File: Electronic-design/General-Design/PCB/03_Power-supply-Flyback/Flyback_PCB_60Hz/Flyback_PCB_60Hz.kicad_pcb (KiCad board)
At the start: 2 copper layers, 150 x 114.2 mm, 88 parts, among them IC1 TPS54302DDCR, IC2 L7812CV, IC3 L7912CV, IC4 DPC817L-A-TR, IC5 UCC38C43DR, IC6 TL431ACLPR, J1 4300.0104, J2 -12V, J3 +12V, J4 +5V, J5 TB002-500-02BE, Q1 BFR182E6327HTSA1, Q3 2N3906BU, Q4 Q_NMOS_GDS, T1 3FS-324, T3 750811351

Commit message: Flyback-PCB-Final1
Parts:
- added ?: , , F.Cu at (28.6, 12.3)
- added ?: , , F.Cu at (100.8, 86.7)
- added ?: , , F.Cu at (27.9, -0.55)
- added ?: , , F.Cu at (108.2, 83.6)
- added ?: , , F.Cu at (32.8, 6.16)
- added ?: , , F.Cu at (29.4, -11.8)
- added ?: , , F.Cu at (93.2, 82.1)
- added FB5: FerriteBead, Flyback:BEADC1608X95N, F.Cu at (99.1, 96.5)
- added REF**: GND_MH, MountingHole:GND_MountingHole, F.Cu at (75.9, 63.3)
- added REF**: GND_MH, MountingHole:GND_MountingHole, F.Cu at (38.8, 10.8)
- added REF**: GND_MH, MountingHole:GND_MountingHole, F.Cu at (96.0, 89.5)
- added REF**: GND_MH, MountingHole:GND_MountingHole, F.Cu at (103.3, 84.1)
- added REF**: GND_MH, MountingHole:GND_MountingHole, F.Cu at (84.2, 78.3)
- added REF**: GND_MH, MountingHole:GND_MountingHole, F.Cu at (90.7, 57.5)
- added REF**: GND_MH, MountingHole:GND_MountingHole, F.Cu at (95.1, 97.4)
- added REF**: GND_MH, MountingHole:GND_MountingHole, F.Cu at (69.6, 84.9)
- added REF**: GND_MH, MountingHole:GND_MountingHole, F.Cu at (101.4, 101.4)
- moved R10 175.2 mm to (86.9, 99.8), turned to 0 degrees
- moved R7 172.9 mm to (81.9, 89.6), turned to -90 degrees
- moved C20 168.3 mm to (64.7, 79.0)
- moved R27 166.3 mm to (90.7, 78.7), turned to -90 degrees
- moved R5 161.1 mm to (98.3, 100.4)
- moved R12 160.9 mm to (93.4, 86.6)
- moved R13 160.0 mm to (93.1, 78.6)
- moved R11 155.9 mm to (100.1, 77.3), turned to 0 degrees
- moved R28 140.7 mm to (82.0, 99.4), turned to 0 degrees
- moved C11 137.9 mm to (65.6, 84.9), turned to 0 degrees
- moved C14 131.7 mm to (83.9, 89.4), turned to -90 degrees
- moved R19 130.0 mm to (85.2, 67.0), turned to 180 degrees
- moved R29 128.6 mm to (109.2, 99.4), turned to 0 degrees
- moved C13 125.8 mm to (91.6, 96.1), turned to 0 degrees
- moved Q3 123.4 mm to (84.6, 84.6)
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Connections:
- J5 pad 1: GND -> Net-(D15-K)
- J5 pad 2: Net-(D15-K) -> GND
- R5 pad 2: Net-(D16-K) -> Net-(FB5-Pad2)
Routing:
- net Net-(BR1-+): track 20.9 -> 192.7 mm
- net Net-(D14-A): track 0.00 -> 87.6 mm
- net Net-(D2-A): track 11.0 -> 78.5 mm
- net Net-(D3-K): track 8.31 -> 73.0 mm
- net Net-(D15-K): track 80.4 -> 143.5 mm
- net Net-(IC5-CS): track 0.00 -> 62.9 mm
- net /Supplies/L: track 72.6 -> 119.5 mm
- net Net-(D14-K): track 0.00 -> 45.1 mm
- net /Supplies/N: track 57.4 -> 100.3 mm
- net Net-(IC4-CATHODE): track 0.00 -> 41.6 mm
- net Net-(T3-AUX_2): track 0.00 -> 39.1 mm
- net Net-(D9-A): track 0.00 -> 37.9 mm
- net Net-(IC6-REF): track 0.00 -> 34.2 mm
- net Net-(IC1-FB): track 0.00 -> 30.1 mm
- net Vref: track 0.00 -> 27.8 mm
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- added copper zone on B.Cu, net GND
- added copper zone on F.Cu, net GND
- added copper zone on B.Cu, net GNDREF
- added copper zone on F.Cu, net GNDREF
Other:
- board size 150 x 114.2 mm -> 174.2 x 124 mm
- board text added: "Prototipo #1 Flyback"

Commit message: Flyback-Ground-plane-completed-1
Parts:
- added ?: , , F.Cu at (41.6, 1.46)
- moved L1 4.37 mm to (50.3, 2.25)
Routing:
- net Net-(D15-A): track 20.1 -> 67.5 mm
- net Net-(D15-K): track 143.5 -> 157.1 mm
- net Net-(IC1-SW): track 18.3 -> 22.6 mm
- net Net-(C3-Pad1): track 22.9 -> 27.3 mm
- net GND: track 31.5 -> 33.7 mm
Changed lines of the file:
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@@
 		(embedded_fonts no)
 	)
+	(footprint ""
+		(layer "F.Cu")
+		(at 41.63 1.46)
+		(property "Reference" ""
+			(at 0 0 0)
+			(layer "F.SilkS")
+			(effects
+				(font
+					(size 1.27 1.27)
+					(thickness 0.15)
+				)
+			)
+		)
+		(property "Value" ""
+			(at 0 0 0)
+			(layer "F.Fab")
+			(effects
+				(font
+					(size 1.27 1.27)
+					(thickness 0.15)
+				)
+			)
+		)
+		(property "Datasheet" ""
+			(at 0 0 0)
+			(layer "F.Fab")
+			(hide yes)
+			(effects
+				(font
+					(size 1.27 1.27)
+					(thickness 0.15)
+				)
+			)
+		)
+		(property "Description" ""
+			(at 0 0 0)
+			(layer "F.Fab")
+			(hide yes)
+			(effects
+				(font
+					(size 1.27 1.27)
+					(thickness 0.15)
+				)
+			)
+		)
+		(pad "1" thru_hole circle
+			(at 0 0)
+			(size 1.5 1.5)
+			(drill 0.65)
+			(layers "*.Cu" "*.Mask")
+			(remove_unused_layers no)
+			(net 6 "GND")
+		)
+		(embedded_fonts no)
+	)
 	(footprint "Flyback:BEADC1608X95N"
 		(layer "F.Cu")
@@
 	(footprint "Footprints_Proyecto:INDPM116102X400N"
 		(layer "F.Cu")
-		(at 45.97 2.24 90)
+		(at 50.34 2.25 90)
 		(descr "AMRM00101040150MA1")
 		(tags "Inductor")
@@
 	)
 	(segment
+		(start 36.872 1.652)
+		(end 36.872 3.61)
+		(width 0.5)
+		(layer "F.Cu")
+		(net 6)
+	)
+	(segment
 		(start 90.68 60.15)
 		(end 90.68 57.57)
@@
 	)
 	(segment
+		(start 36.68 1.46)
+		(end 36.872 1.652)
+		(width 0.5)
+		(layer "F.Cu")
+		(net 6)
+	)
+	(segment
 		(start 90.68 57.57)
 		(end 90.71 57.54)
@@
 	)
 	(segment
-		(start 45.97 -2.36)
-		(end 35.735242 -2.36)
+		(start 31.947621 -5.3)
+		(end 31.907621 -5.26)
 		(width 1)
 		(layer "F.Cu")
@@
 	)
 	(segment
-		(start 31.947621 -5.3)
-		(end 31.907621 -5.26)
-		(width 1)
+		(start 35.745242 -2.35)
+		(end 35.347621 -2.747621)
+		(width 1.1)
 		(layer "F.Cu")
 		(net 8)
@@
 	)
 	(segment
+		(start 50.34 -2.35)
+		(end 35.745242 -2.35)
+		(width 1.1)
+		(layer "F.Cu")
+		(net 8)
+	)
+	(segment
 		(start 35.347621 -2.747621)
 		(end 35.347621 -5.33)
@@
 	)
 	(segment
-		(start 35.735242 -2.36)
-		(end 35.347621 -2.747621)
-		(width 1)
-		(layer "F.Cu")
-		(net 8)
-	)
-	(segment
 		(start 34.67 6.11)
 		(end 32.8 6.11)
@@
 	)
 	(segment
+		(start 40.02 6.85)
+		(end 38.03 4.86)
+		(width 1.1)
+		(layer "F.Cu")
+		(net 10)
+	)
+	(segment
 		(start 35.69 4.42)
 		(end 35.69 4.14705)
@@
 	)
 	(segment
-		(start 40.01 6.84)
-		(end 45.97 6.84)
-		(width 1)
-		(layer "F.Cu")
-		(net 10)
-	)
-	(segment
-		(start 37.82 4.86)
-		(end 38.03 4.86)
-		(width 1)
-		(layer "F.Cu")
-		(net 10)
-	)
-	(segment
 		(start 36.13 4.86)
 		(end 32.29 4.86)
@@
 	(segment
 		(start 38.03 4.86)
-		(end 40.01 6.84)
-		(width 1)
+		(end 37.82 4.86)
+		(width 1.1)
 		(layer "F.Cu")
 		(net 10)
@@
 	)
 	(segment
+		(start 50.34 6.85)
+		(end 40.02 6.85)
+		(width 1.1)
+		(layer "F.Cu")
+		(net 10)
+	)
+	(segment
 		(start 36.13 4.86)
 		(end 37.82 4.86)
@@
 	)
 	(segment
+		(start 159.24 43.33)
+		(end 159.59 42.98)
+		(width 3.5)
+		(layer "F.Cu")
+		(net 25)
+	)
+	(segment
 		(start 86.77 66.99)
 		(end 94.12 66.99)
@@
 	)
 	(segment
+		(start 159.24 48.09)
+		(end 160.31 48.09)
+		(width 3.5)
+		(layer "F.Cu")
+		(net 25)
+	)
+	(segment
+		(start 159.24 48.09)
+		(end 159.24 43.33)
+		(width 3.5)
+		(layer "F.Cu")
+		(net 25)
+	)
+	(segment
 		(start 145.08 42.98)
 		(end 144.8 42.7)
@@
 	)
 	(segment
+		(start 160.31 48.09)
+		(end 165.42 42.98)
+		(width 3.5)
+		(layer "F.Cu")
+		(net 25)
+	)
+	(segment
 		(start 165.42 42.98)
-		(end 145.08 42.98)
+		(end 159.59 42.98)
 		(width 4.5)
 		(layer "F.Cu")
@@
 	)
 	(segment
+		(start 159.59 42.98)
+		(end 145.08 42.98)
+		(width 4.5)
+		(layer "F.Cu")
+		(net 25)
+	)
+	(segment
 		(start 145.08 42.98)
 		(end 144.8 42.7)
@@
 	)
 	(segment
+		(start 144.5 54.26)
+		(end 150.67 48.09)
+		(width 4.5)
+		(layer "F.Cu")
+		(net 33)
+	)
+	(segment
+		(start 154.639 58.971)
+		(end 154.639 48.09)
+		(width 4.5)
+		(layer "F.Cu")
+		(net 33)
+	)
+	(segment
+		(start 149.5 61.44)
+		(end 149.5 49.26)
+		(width 4.5)
+		(layer "F.Cu")
+		(net 33)
+	)
+	(segment
+		(start 154.5 61.44)
+		(end 154.5 59.11)
+		(width 4.5)
+		(layer "F.Cu")
+		(net 33)
+	)
+	(segment
+		(start 149.5 49.26)
+		(end 150.67 48.09)
+		(width 4.5)
+		(layer "F.Cu")
+		(net 33)
+	)
+	(segment
 		(start 144.5 61.39)
 		(end 144.55 61.44)
@@
 	)
 	(segment
+		(start 144.5 61.44)
+		(end 144.5 54.26)
+		(width 4.5)
+		(layer "F.Cu")
+		(net 33)
+	)
+	(segment
+		(start 154.5 59.11)
+		(end 154.639 58.971)
+		(width 4.5)
+		(layer "F.Cu")
+		(net 33)
+	)
+	(segment
 		(start 144.55 61.44)
 		(end 154.5 61.44)
@@
 	)
 	(segment
+		(start 150.67 48.09)
+		(end 154.94 48.09)
+		(width 4.5)
+		(layer "F.Cu")
+		(net 33)
+	)
+	(segment
 		(start 154.5 61.44)
 		(end 144.5 61.44)
@@
 		(polygon
 			(pts
-				(xy 85.595059 87.753512) (xy 95.956149 87.71794) (xy 96.047844 101.955014) (xy 85.615112 101.919264)
+				(xy 85.595059 87.753512) (xy 95.956149 87.71794) (xy 96.003572 95.081144) (xy 85.605382 95.045513)
 			)
 		)
@@
 		(polygon
 			(pts
-				(xy 40.12 -4.81) (xy 51.77 -4.85) (xy 51.860463 9.197397) (xy 40.139769 9.157227)
+				(xy 44.49 -4.8) (xy 56.14 -4.84) (xy 56.230463 9.207397) (xy 44.509769 9.167227)
 			)
 		)

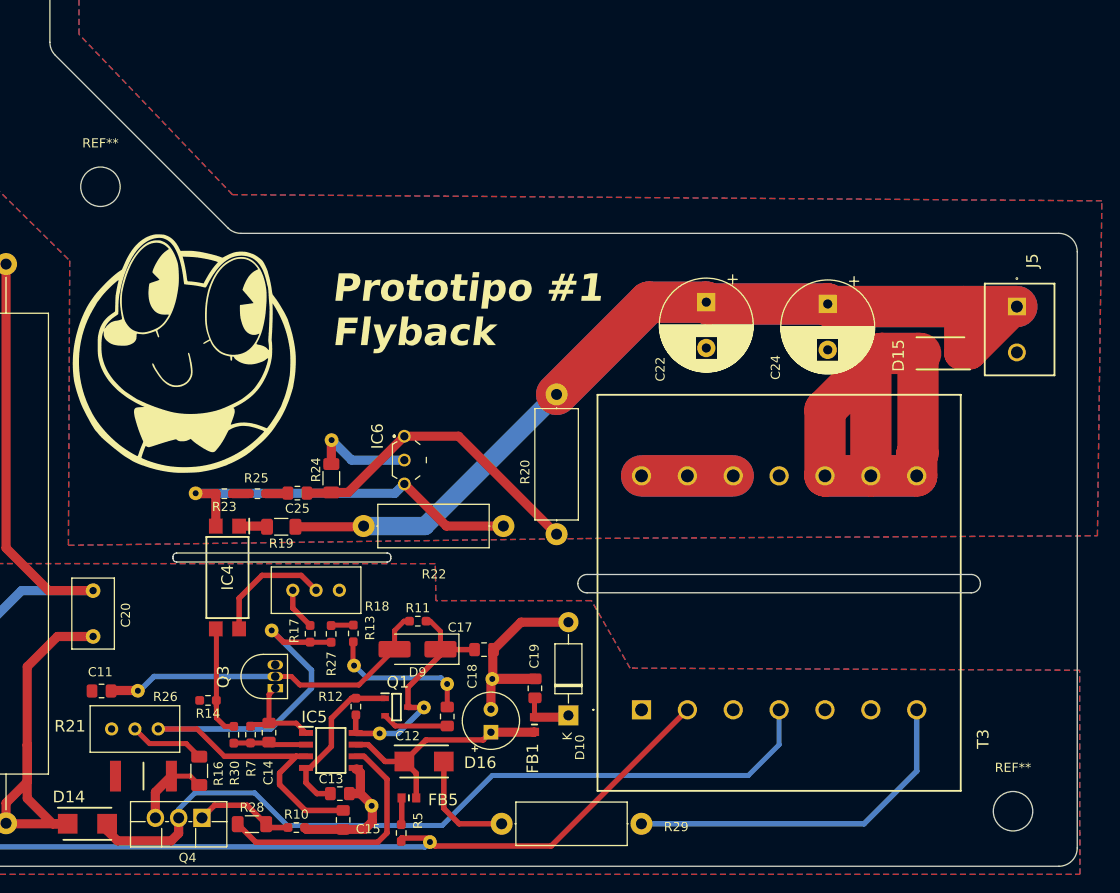
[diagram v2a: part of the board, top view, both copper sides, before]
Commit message: Flyback-sch-correction
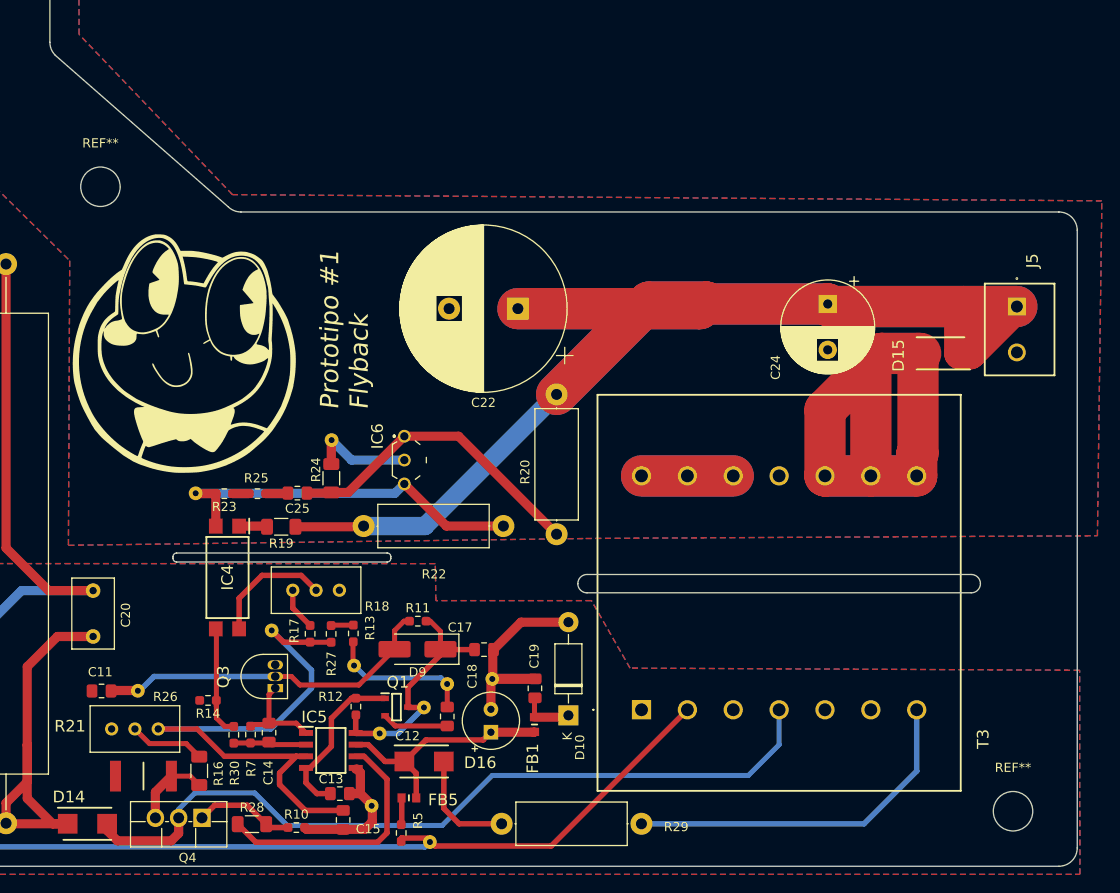
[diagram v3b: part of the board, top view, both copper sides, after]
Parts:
- C22: value 680uF -> 330uF; footprint Capacitor_THT:CP_Radial_D10.0mm_P5.00mm -> Capacitor_THT:CP_Radial_D18.0mm_P7.50mm
- moved C22 20.6 mm to (111.0, 43.2), turned to 180 degrees
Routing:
- net Net-(D15-K): track 157.1 -> 198.8 mm
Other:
- outline, holes or cut-outs redrawn

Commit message: Flyback-sch-correction2
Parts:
- added R6: 4k, Resistor_THT:R_Axial_Power_L20.0mm_W6.4mm_P25.40mm, F.Cu at (55.2, 69.2)
- R9: value 50k -> 4k; footprint Resistor_THT:R_Axial_Power_L50.0mm_W9.0mm_P60.96mm -> Resistor_THT:R_Axial_Power_L20.0mm_W6.4mm_P25.40mm
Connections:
- R9 pad 2: Net-(BR1-+) -> Net-(R6-Pad1)
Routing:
- net Net-(BR1-+): track 192.7 -> 215.4 mm
- net Net-(R6-Pad1): track 0.00 -> 9.26 mm
